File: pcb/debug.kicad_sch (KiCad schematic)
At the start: 0 parts

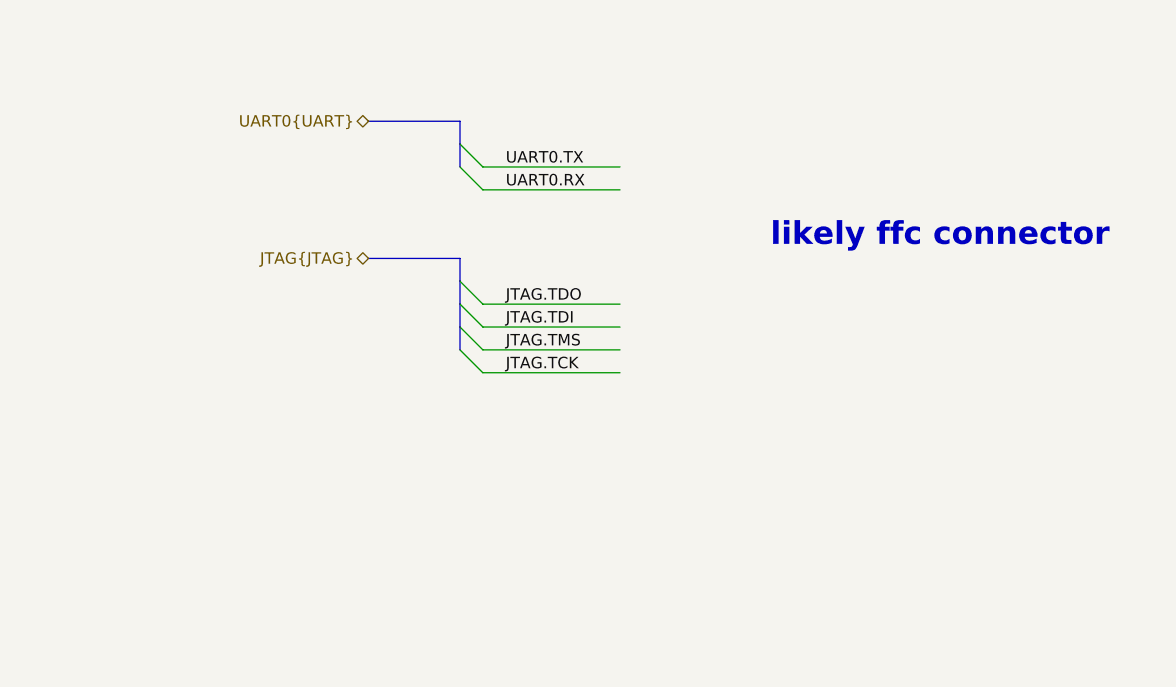
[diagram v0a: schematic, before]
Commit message: phy and debug ffc conn
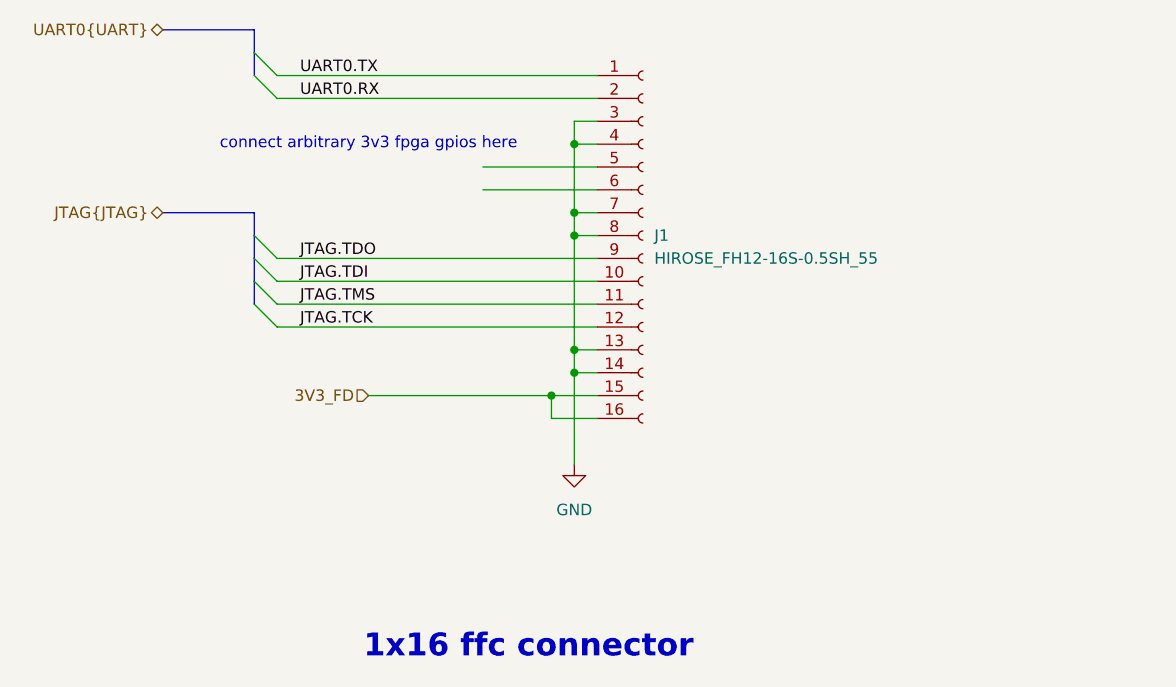
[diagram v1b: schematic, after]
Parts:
- added J1: HIROSE_FH12-16S-0.5SH_55, library:HIROSE_FH12-16S-0.5SH_55_, symbol Connector:Conn_01x16_Socket
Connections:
- net JTAG.TCK: now also J1.12 (Pin_12)
- net JTAG.TDI: now also J1.10 (Pin_10)
- net JTAG.TDO: now also J1.9 (Pin_9)
- net JTAG.TMS: now also J1.11 (Pin_11)
- net UART0.RX: now also J1.2 (Pin_2)
- net UART0.TX: now also J1.1 (Pin_1)
- new net 3V3_FD: J1.15 (Pin_15), J1.16 (Pin_16)
- new net GND: J1.13 (Pin_13), J1.14 (Pin_14), J1.3 (Pin_3), J1.4 (Pin_4), J1.7 (Pin_7), J1.8 (Pin_8)
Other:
- note added: "1x16 ffc connector"
- note added: "connect arbitrary 3v3 fpga gpios here"
- note removed: "likely ffc connector"
